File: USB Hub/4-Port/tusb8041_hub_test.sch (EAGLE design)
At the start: 116 parts

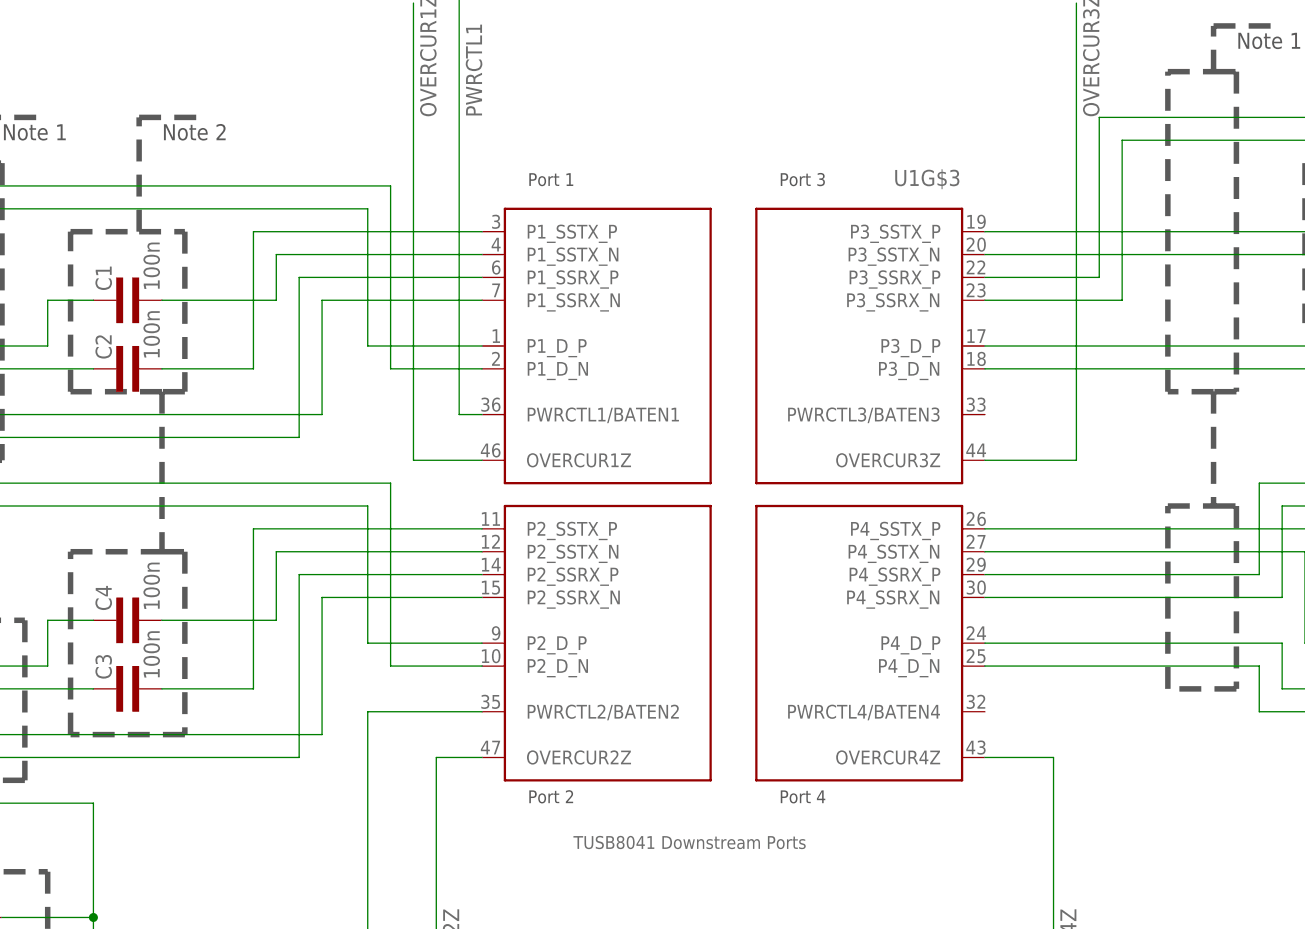
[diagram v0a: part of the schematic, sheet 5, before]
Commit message: Changes from surface book
These are the files that have changed on the surface book. I have not tracked the project individually.
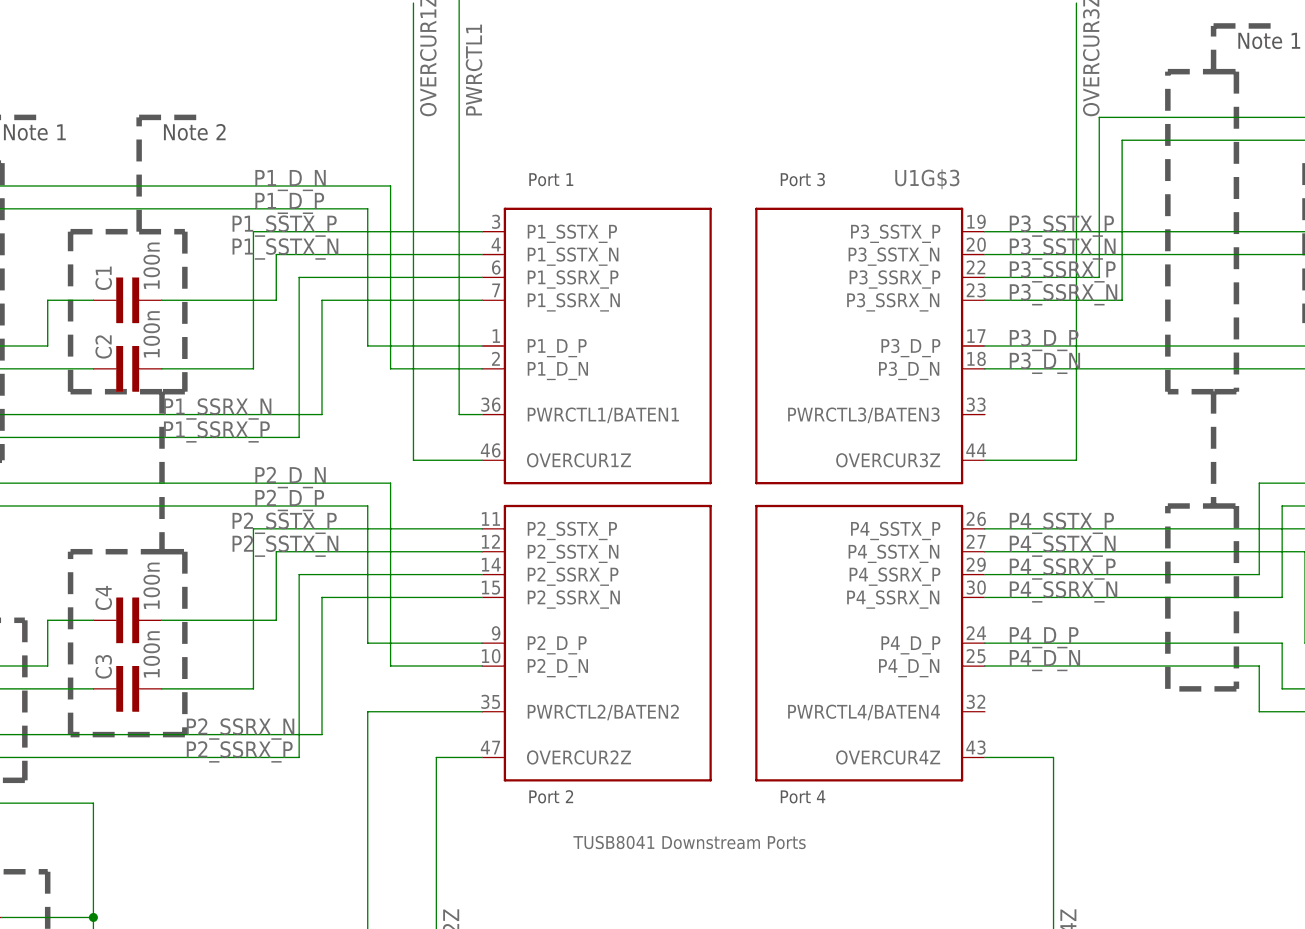
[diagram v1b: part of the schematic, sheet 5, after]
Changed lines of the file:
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@@
 <?xml version="1.0" encoding="utf-8"?>
 <!DOCTYPE eagle SYSTEM "eagle.dtd">
-<eagle version="6.4">
+<eagle version="9.0.0">
 <drawing>
 <settings>
 <setting alwaysvectorfont="no"/>
+<setting keepoldvectorfont="yes"/>
 <setting verticaltext="up"/>
 </settings>
@@
 <pinref part="C29" gate="G$1" pin="1"/>
 <wire x1="27.94" y1="43.18" x2="30.48" y2="43.18" width="0.1524" layer="91"/>
+<label x="5.08" y="40.64" size="1.778" layer="95"/>
 </segment>
 </net>
@@
 <pinref part="C30" gate="G$1" pin="1"/>
 <wire x1="27.94" y1="35.56" x2="30.48" y2="35.56" width="0.1524" layer="91"/>
+<label x="5.08" y="38.1" size="1.778" layer="95"/>
 </segment>
 </net>
@@
 <pinref part="C29" gate="G$1" pin="2"/>
 <wire x1="40.64" y1="43.18" x2="38.1" y2="43.18" width="0.1524" layer="91"/>
+<label x="43.18" y="53.34" size="1.778" layer="95"/>
 </segment>
 </net>
@@
 <pinref part="C30" gate="G$1" pin="2"/>
 <wire x1="43.18" y1="35.56" x2="38.1" y2="35.56" width="0.1524" layer="91"/>
+<label x="43.18" y="50.8" size="1.778" layer="95"/>
 </segment>
 </net>
@@
 <pinref part="JP5" gate="G$1" pin="STDB_SSRX-"/>
 <wire x1="15.24" y1="33.02" x2="5.08" y2="33.02" width="0.1524" layer="91"/>
+<label x="17.78" y="25.4" size="1.778" layer="95"/>
 </segment>
 </net>
@@
 <pinref part="JP5" gate="G$1" pin="STDB_SSRX+"/>
 <wire x1="12.7" y1="30.48" x2="5.08" y2="30.48" width="0.1524" layer="91"/>
+<label x="15.24" y="22.86" size="1.778" layer="95"/>
 </segment>
 </net>
@@
 <pinref part="JP5" gate="G$1" pin="D+"/>
 <wire x1="17.78" y1="45.72" x2="5.08" y2="45.72" width="0.1524" layer="91"/>
+<label x="20.32" y="27.94" size="1.778" layer="95"/>
 </segment>
 </net>
@@
 <pinref part="JP5" gate="G$1" pin="D-"/>
 <wire x1="20.32" y1="48.26" x2="5.08" y2="48.26" width="0.1524" layer="91"/>
+<label x="22.86" y="30.48" size="1.778" layer="95"/>
 </segment>
 </net>
@@
 <wire x1="43.18" y1="71.12" x2="43.18" y2="73.66" width="0.1524" layer="91"/>
 <junction x="43.18" y="73.66"/>
+<label x="71.12" y="73.66" size="1.778" layer="95"/>
 </segment>
 <segment>
@@
 <pinref part="C2" gate="G$1" pin="2"/>
 <wire x1="10.16" y1="55.88" x2="20.32" y2="55.88" width="0.1524" layer="91"/>
+<label x="17.78" y="71.12" size="1.778" layer="95"/>
 </segment>
 </net>
@@
 <pinref part="C1" gate="G$1" pin="2"/>
 <wire x1="22.86" y1="63.5" x2="10.16" y2="63.5" width="0.1524" layer="91"/>
+<label x="17.78" y="68.58" size="1.778" layer="95"/>
 </segment>
 </net>
@@
 <pinref part="JP1" gate="G$1" pin="STDA_SSRX+"/>
 <wire x1="25.4" y1="48.26" x2="-35.56" y2="48.26" width="0.1524" layer="91"/>
+<label x="10.16" y="48.26" size="1.778" layer="95"/>
 </segment>
 </net>
@@
 <pinref part="JP1" gate="G$1" pin="STDA_SSRX-"/>
 <wire x1="27.94" y1="50.8" x2="-35.56" y2="50.8" width="0.1524" layer="91"/>
+<label x="10.16" y="50.8" size="1.778" layer="95"/>
 </segment>
 </net>
@@
 <pinref part="JP1" gate="G$1" pin="D+"/>
 <wire x1="-22.86" y1="63.5" x2="-35.56" y2="63.5" width="0.1524" layer="91"/>
+<label x="20.32" y="73.66" size="1.778" layer="95"/>
 </segment>
 </net>
@@
 <pinref part="JP1" gate="G$1" pin="D-"/>
 <wire x1="-25.4" y1="66.04" x2="-35.56" y2="66.04" width="0.1524" layer="91"/>
+<label x="20.32" y="76.2" size="1.778" layer="95"/>
 </segment>
 </net>
@@
 <pinref part="C4" gate="G$1" pin="2"/>
 <wire x1="10.16" y1="27.94" x2="22.86" y2="27.94" width="0.1524" layer="91"/>
+<label x="17.78" y="35.56" size="1.778" layer="95"/>
 </segment>
 </net>
@@
 <pinref part="JP2" gate="G$1" pin="STDA_SSRX+"/>
 <wire x1="25.4" y1="12.7" x2="-35.56" y2="12.7" width="0.1524" layer="91"/>
+<label x="12.7" y="12.7" size="1.778" layer="95"/>
 </segment>
 </net>
@@
 <pinref part="JP2" gate="G$1" pin="STDA_SSRX-"/>
 <wire x1="27.94" y1="15.24" x2="-35.56" y2="15.24" width="0.1524" layer="91"/>
+<label x="12.7" y="15.24" size="1.778" layer="95"/>
 </segment>
 </net>
@@
 <pinref part="JP2" gate="G$1" pin="D+"/>
 <wire x1="-22.86" y1="27.94" x2="-35.56" y2="27.94" width="0.1524" layer="91"/>
+<label x="20.32" y="40.64" size="1.778" layer="95"/>
 </segment>
 </net>
@@
 <pinref part="JP2" gate="G$1" pin="D-"/>
 <wire x1="-25.4" y1="30.48" x2="-35.56" y2="30.48" width="0.1524" layer="91"/>
+<label x="20.32" y="43.18" size="1.778" layer="95"/>
 </segment>
 </net>
@@
 <pinref part="C3" gate="G$1" pin="2"/>
 <wire x1="10.16" y1="20.32" x2="20.32" y2="20.32" width="0.1524" layer="91"/>
+<label x="17.78" y="38.1" size="1.778" layer="95"/>
 </segment>
 </net>
@@
 <pinref part="JP3" gate="G$1" pin="STDA_SSRX+"/>
 <wire x1="175.26" y1="71.12" x2="187.96" y2="71.12" width="0.1524" layer="91"/>
+<label x="104.14" y="66.04" size="1.778" layer="95"/>
 </segment>
 </net>
@@
 <pinref part="JP3" gate="G$1" pin="STDA_SSRX-"/>
 <wire x1="172.72" y1="68.58" x2="187.96" y2="68.58" width="0.1524" layer="91"/>
+<label x="104.14" y="63.5" size="1.778" layer="95"/>
 </segment>
 </net>
@@
 <pinref part="JP3" gate="G$1" pin="D+"/>
 <wire x1="152.4" y1="55.88" x2="187.96" y2="55.88" width="0.1524" layer="91"/>
+<label x="104.14" y="58.42" size="1.778" layer="95"/>
 </segment>
 </net>
@@
 <pinref part="JP3" gate="G$1" pin="D-"/>
 <wire x1="149.86" y1="53.34" x2="187.96" y2="53.34" width="0.1524" layer="91"/>
+<label x="104.14" y="55.88" size="1.778" layer="95"/>
 </segment>
 </net>
@@
 <pinref part="C13" gate="G$1" pin="1"/>
 <wire x1="142.24" y1="25.4" x2="137.16" y2="25.4" width="0.1524" layer="91"/>
+<label x="104.14" y="35.56" size="1.778" layer="95"/>
 </segment>
 </net>
@@
 <pinref part="JP4" gate="G$1" pin="STDA_SSRX+"/>
 <wire x1="175.26" y1="35.56" x2="187.96" y2="35.56" width="0.1524" layer="91"/>
+<label x="104.14" y="33.02" size="1.778" layer="95"/>
 </segment>
 </net>
@@
 <pinref part="JP4" gate="G$1" pin="STDA_SSRX-"/>
 <wire x1="172.72" y1="33.02" x2="187.96" y2="33.02" width="0.1524" layer="91"/>
+<label x="104.14" y="30.48" size="1.778" layer="95"/>
 </segment>
 </net>
@@
 <pinref part="JP4" gate="G$1" pin="D+"/>
 <wire x1="134.62" y1="20.32" x2="187.96" y2="20.32" width="0.1524" layer="91"/>
+<label x="104.14" y="25.4" size="1.778" layer="95"/>
 </segment>
 </net>
@@
 <pinref part="JP4" gate="G$1" pin="D-"/>
 <wire x1="132.08" y1="17.78" x2="187.96" y2="17.78" width="0.1524" layer="91"/>
+<label x="104.14" y="22.86" size="1.778" layer="95"/>
 </segment>
 </net>
@@
 <pinref part="C9" gate="G$1" pin="1"/>
 <wire x1="101.6" y1="71.12" x2="142.24" y2="71.12" width="0.1524" layer="91"/>
+<label x="104.14" y="71.12" size="1.778" layer="95"/>
 </segment>
 </net>
@@
 <pinref part="C10" gate="G$1" pin="1"/>
 <wire x1="139.7" y1="63.5" x2="142.24" y2="63.5" width="0.1524" layer="91"/>
+<label x="104.14" y="68.58" size="1.778" layer="95"/>
 </segment>
 </net>
@@
 <wire x1="142.24" y1="33.02" x2="139.7" y2="33.02" width="0.1524" layer="91"/>
 <wire x1="139.7" y1="33.02" x2="139.7" y2="38.1" width="0.1524" layer="91"/>
-</segment>
-</net>
+<label x="104.14" y="38.1" size="1.778" layer="95"/>
+</segment>
+</net>

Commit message: Several Projects
Projects - Vape - USB Microphone - USB Hub - Headphone Amps - Backpack
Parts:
- added R19, R20: 4.7K, common:RES0402L3
- CN2: value (none) -> BRD_5V
- LED1: value (none) -> VBUS1
- LED2: value (none) -> VBUS2
- LED3: value (none) -> VBUS3
- LED4: value (none) -> VBUS4
- LED5: value (none) -> PWR
- LED6: value (none) -> SS_UP
- LED7: value (none) -> HS_UP
- R10, R16, R18, R6, R8, R9: value (none) -> 220R
- U1: value (none) -> USB_HUB
- U2, U3, U4, U5: value (none) -> USB_5V
- U6: value (none) -> BRD_3V3
- U8: value (none) -> BRD_1V1
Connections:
- net PWRCTL3: now also R20.2, U1G$3.PWRCTL3/BATEN3
- net PWRCTL4: now also R19.2, U1G$3.PWRCTL4/BATEN4
- net VDD33: now also R19.1, R20.1
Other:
- moved on the sheet: C46, C47, C48, C49
